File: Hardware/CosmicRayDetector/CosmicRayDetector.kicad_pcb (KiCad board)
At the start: 2 copper layers, 40 x 70 mm, 34 parts, among them J1 Conn_01x01_Female, J10 Conn_01x01_Female, J11 Conn_01x01_Female, J2 Conn_01x02, J6 Conn_01x04, J8 Conn_01x01_Female, J9 Conn_01x01_Female, U1 HEF4093B

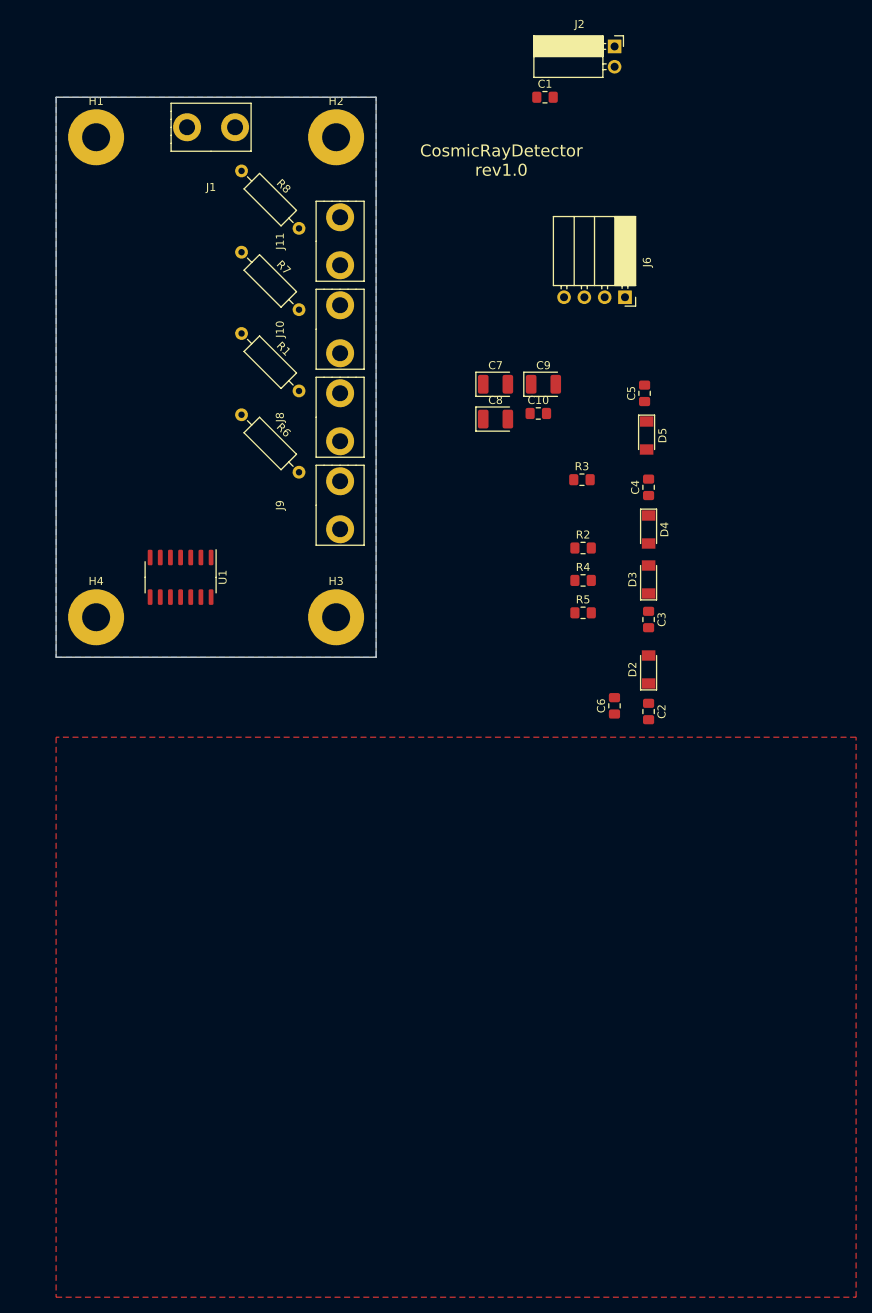
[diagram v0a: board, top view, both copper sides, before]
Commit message: done component placement on pcb and a draft of routing
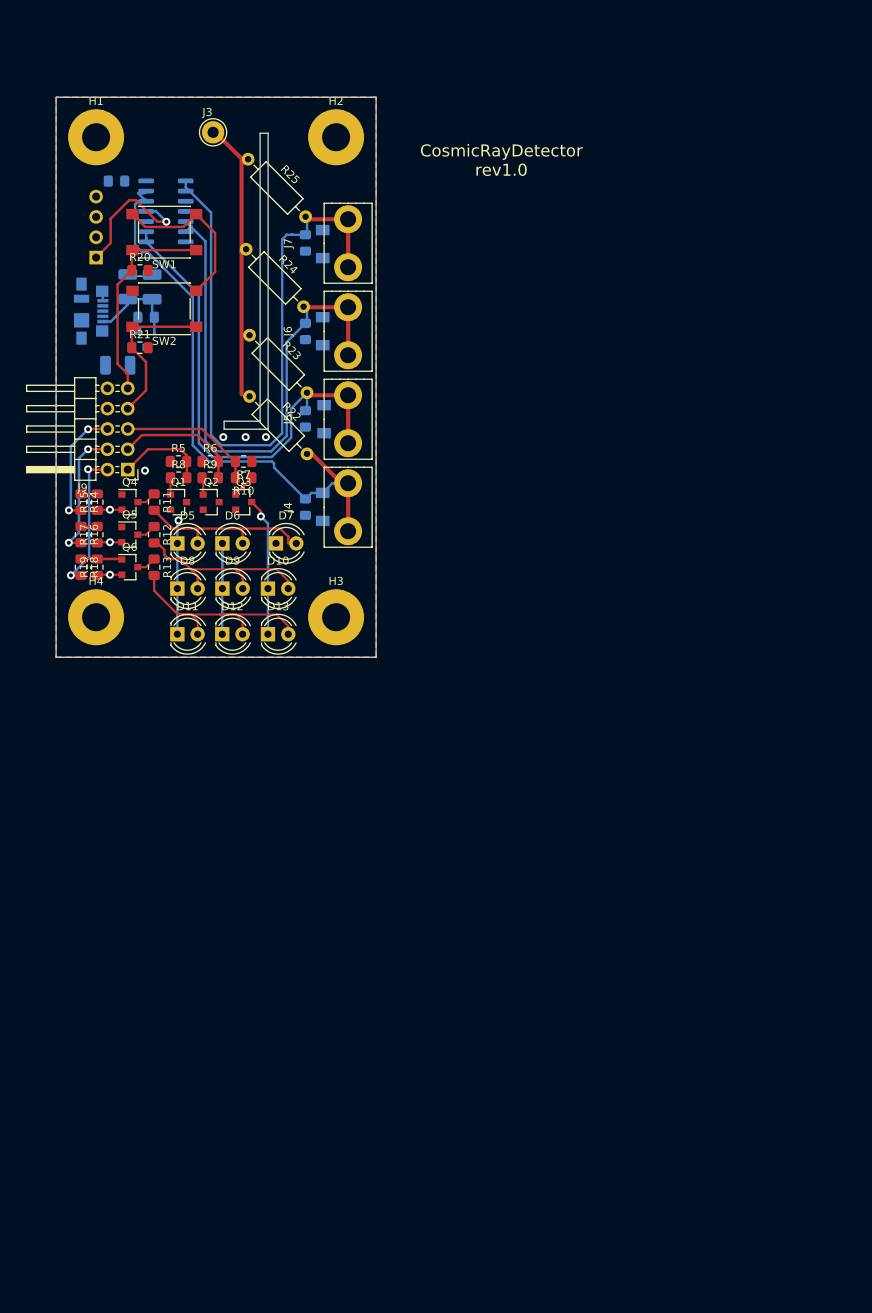
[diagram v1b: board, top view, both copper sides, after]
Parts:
- removed C10: 100n, Capacitor_SMD:C_0805_2012Metric_Pad1.15x1.40mm_HandSolder
- removed C2, C3, C4: 220p, Capacitor_SMD:C_0805_2012Metric_Pad1.15x1.40mm_HandSolder
- removed the C5 at (93.6, 57.0)
- removed J11: Conn_01x01_Female, CosmicRayDetector:GeigerTube
- removed J2: Conn_01x02, Connector_PinSocket_2.54mm:PinSocket_1x02_P2.54mm_Horizontal
- removed the J6 at (91.1, 45.0)
- added D1: 5V1, Diode_SMD:D_MiniMELF, B.Cu at (53.3, 71.2)
- added D10: LED, LED_THT:LED_D4.0mm, F.Cu at (46.5, 81.4)
- added D11: LED, LED_THT:LED_D4.0mm, F.Cu at (35.2, 87.1)
- added D12: LED, LED_THT:LED_D4.0mm, F.Cu at (40.8, 87.1)
- added D13: LED, LED_THT:LED_D4.0mm, F.Cu at (46.5, 87.1)
- added D6: LED, LED_THT:LED_D4.0mm, F.Cu at (40.8, 75.8)
- added D7: LED, LED_THT:LED_D4.0mm, F.Cu at (47.5, 75.8)
- added D8: LED, LED_THT:LED_D4.0mm, F.Cu at (35.2, 81.4)
- added D9: LED, LED_THT:LED_D4.0mm, F.Cu at (40.8, 81.4)
- added J1: Conn_01x04, Connector_PinSocket_2.54mm:PinSocket_1x04_P2.54mm_Horizontal, B.Cu at (25.0, 40.0)
- added J7: Conn_01x01_Female, CosmicRayDetector:GeigerTube, F.Cu at (48.5, 38.2)
- added J8: USB_B_Micro, Connector_USB:USB_Micro-B_Molex_47346-0001, B.Cu at (24.4, 46.7)
- added J9: Conn_02x05_Odd_Even, Connector_PinHeader_2.54mm:PinHeader_2x05_P2.54mm_Horizontal, F.Cu at (29.0, 66.5)
- added Q1: BC848, Package_TO_SOT_SMD:SOT-23, F.Cu at (35.3, 70.6)
- added Q2: BC848, Package_TO_SOT_SMD:SOT-23, F.Cu at (39.4, 70.6)
- added Q3: BC848, Package_TO_SOT_SMD:SOT-23, F.Cu at (43.5, 70.6)
- added Q4: BC859, Package_TO_SOT_SMD:SOT-23, F.Cu at (29.2, 70.6)
- added Q5: BC859, Package_TO_SOT_SMD:SOT-23, F.Cu at (29.2, 74.7)
- added Q6: BC859, Package_TO_SOT_SMD:SOT-23, F.Cu at (29.2, 78.7)
- added R10: 10k, Resistor_SMD:R_0805_2012Metric_Pad1.15x1.40mm_HandSolder, F.Cu at (43.4, 67.6)
- added R11: 10k, Resistor_SMD:R_0805_2012Metric_Pad1.15x1.40mm_HandSolder, F.Cu at (32.3, 70.6)
- added R12: 10k, Resistor_SMD:R_0805_2012Metric_Pad1.15x1.40mm_HandSolder, F.Cu at (32.3, 74.7)
- added R13: 10k, Resistor_SMD:R_0805_2012Metric_Pad1.15x1.40mm_HandSolder, F.Cu at (32.3, 78.7)
- added R14: 10k, Resistor_SMD:R_0805_2012Metric_Pad1.15x1.40mm_HandSolder, F.Cu at (23.1, 70.6)
- added R15: 10k, Resistor_SMD:R_0805_2012Metric_Pad1.15x1.40mm_HandSolder, F.Cu at (25.1, 70.6)
- added R16: 10k, Resistor_SMD:R_0805_2012Metric_Pad1.15x1.40mm_HandSolder, F.Cu at (23.1, 74.7)
- added R17: 10k, Resistor_SMD:R_0805_2012Metric_Pad1.15x1.40mm_HandSolder, F.Cu at (25.1, 74.7)
- added R18: 10k, Resistor_SMD:R_0805_2012Metric_Pad1.15x1.40mm_HandSolder, F.Cu at (23.1, 78.7)
- added R19: 10k, Resistor_SMD:R_0805_2012Metric_Pad1.15x1.40mm_HandSolder, F.Cu at (25.1, 78.7)
- added R2: 10k, Resistor_SMD:R_0805_2012Metric_Pad1.15x1.40mm_HandSolder, B.Cu at (51.2, 60.2)
- added R20: 10k, Resistor_SMD:R_0805_2012Metric_Pad1.15x1.40mm_HandSolder, F.Cu at (30.5, 41.7)
- added R21: 10k, Resistor_SMD:R_0805_2012Metric_Pad1.15x1.40mm_HandSolder, F.Cu at (30.5, 51.3)
- added R6: 10k, Resistor_SMD:R_0805_2012Metric_Pad1.15x1.40mm_HandSolder, F.Cu at (39.3, 65.5)
- added R7: 10k, Resistor_SMD:R_0805_2012Metric_Pad1.15x1.40mm_HandSolder, F.Cu at (43.4, 65.5)
- added R8: 10k, Resistor_SMD:R_0805_2012Metric_Pad1.15x1.40mm_HandSolder, F.Cu at (35.3, 67.6)
- added R9: 10k, Resistor_SMD:R_0805_2012Metric_Pad1.15x1.40mm_HandSolder, F.Cu at (39.3, 67.6)
- added SW1: SW_Push, Button_Switch_SMD:SW_SPST_PTS645, F.Cu at (33.5, 36.9)
- added SW2: SW_Push, Button_Switch_SMD:SW_SPST_PTS645, F.Cu at (33.5, 46.4)
- added U2: AZ1117-3.3, Package_TO_SOT_SMD:SOT-23, B.Cu at (30.2, 50.2)
- C5: renamed from C6; moved to B.Cu
- C6: renamed from C1; moved to B.Cu
- C7, C8, C9, D2, D3, D4, R3, R4, U1: moved to B.Cu
- D5: value 5V1 -> LED; footprint Diode_SMD:D_MiniMELF -> LED_THT:LED_D4.0mm
- J3: renamed from J1; footprint CosmicRayDetector:GeigerTube -> TestPoint:TestPoint_Loop_D2.60mm_Drill1.4mm_Beaded
- R1: renamed from R2; moved to B.Cu
- moved C5 90.4 mm to (27.6, 30.5), turned to 180 degrees
- moved D5 60.2 mm to (35.2, 75.8), turned to 0 degrees
- moved C6 56.9 mm to (31.2, 47.5), turned to 180 degrees
- moved R4 54.6 mm to (51.2, 38.2), turned to 270 degrees
- moved D4 54.2 mm to (53.3, 38.4)
- moved R5 54.0 mm to (35.3, 65.5)
- moved C9 53.3 mm to (27.7, 53.5), turned to 180 degrees
- moved D2 51.2 mm to (53.5, 60.2), turned to 270 degrees
- moved D3 51.2 mm to (53.3, 49.2), turned to 270 degrees
- moved C8 48.9 mm to (29.0, 43.7), turned to 90 degrees
- moved U1 45.8 mm to (33.7, 34.3), turned to 180 degrees
- moved C7 44.6 mm to (32.0, 43.7), turned to 90 degrees
- moved R3 39.2 mm to (51.2, 49.3), turned to 270 degrees
- moved R1 35.1 mm to (51.2, 71.2), turned to 270 degrees
- moved J4 11.3 mm to (48.5, 71.2)
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- renumbered J8 to J4, J9 to J5, J10 to J6, R1 to R22, R6 to R23, R7 to R24, R8 to R25
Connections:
- C5 pad 1: VCC -> +3V3
- D2 pad 1: GM_CONNECTOR_1 -> GM_CONNECTOR_2
- D3 pad 1: GM_CONNECTOR_2 -> GM_CONNECTOR_3
- D4 pad 1: GM_CONNECTOR_3 -> GM_CONNECTOR_4
- D5 pad 1: GM_CONNECTOR_4 -> Net-(D11-Pad1)
- D5 pad 2: GND -> Net-(D5-Pad2)
- R3 pad 1: GM_CONNECTOR_2 -> GM_CONNECTOR_3
- R4 pad 1: GM_CONNECTOR_3 -> GM_CONNECTOR_4
- R5 pad 1: GM_CONNECTOR_4 -> GND
- R5 pad 2: GND -> /UserInterface/LED_X_3
- U1 pad 1: GM_CONNECTOR_3 -> GM_CONNECTOR_4
- U1 pad 10: GM1 -> Net-(J1-Pad2)
- U1 pad 11: GM2 -> Net-(J1-Pad1)
- U1 pad 12: GM_CONNECTOR_2 -> GM_CONNECTOR_1
- U1 pad 13: GM_CONNECTOR_2 -> GM_CONNECTOR_1
- U1 pad 14: VCC -> +3V3
- U1 pad 2: GM_CONNECTOR_3 -> GM_CONNECTOR_4
- U1 pad 3: GM3 -> Net-(J1-Pad4)
- U1 pad 4: GM4 -> Net-(J1-Pad3)
- U1 pad 5: GM_CONNECTOR_4 -> GM_CONNECTOR_3
- U1 pad 6: GM_CONNECTOR_4 -> GM_CONNECTOR_3
- U1 pad 8: GM_CONNECTOR_1 -> GM_CONNECTOR_2
- U1 pad 9: GM_CONNECTOR_1 -> GM_CONNECTOR_2
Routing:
- net GM_CONNECTOR_4: track 0.00 -> 85.1 mm
- net GM_CONNECTOR_1: track 0.00 -> 73.9 mm
- net GM_CONNECTOR_3: track 0.00 -> 70.3 mm
- net GM_CONNECTOR_2: track 0.00 -> 63.6 mm
- net Net-(J3-Pad1): track 0.00 -> 33.9 mm
- net Net-(D11-Pad2): track 0.00 -> 30.8 mm
- net /UserInterface/BUTTON_1: track 0.00 -> 26.5 mm
- net Net-(D10-Pad2): track 0.00 -> 25.6 mm
- net Net-(D5-Pad2): track 0.00 -> 23.9 mm
- net +5V: track 0.00 -> 23.8 mm, vias 0 -> 3
- net +3V3: track 0.00 -> 20.8 mm
- net /UserInterface/BUTTON_2: track 0.00 -> 19.9 mm
- net /UserInterface/LED_Y_3: track 0.00 -> 18.3 mm, vias 0 -> 2
- net Net-(J1-Pad1): track 0.00 -> 17.7 mm, vias 0 -> 1
- net Net-(D10-Pad1): track 0.00 -> 17.4 mm, vias 0 -> 1
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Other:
- outline, holes or cut-outs redrawn
- net class Default: clearance 0.254 -> 0.1778
- net class high voltage: clearance 2 -> 0.254; trace_width 0.3048 -> 2
- rule trace_clearance: 0.254 -> 0.1778

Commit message: finished pcb design
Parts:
- removed J9: Conn_02x05_Odd_Even, Connector_PinHeader_2.54mm:PinHeader_2x05_P2.54mm_Horizontal
- added C2: 100n, Capacitor_SMD:C_0805_2012Metric_Pad1.15x1.40mm_HandSolder, F.Cu at (30.0, 65.5)
- added D14: LED, LED_THT:LED_D4.0mm, F.Cu at (34.5, 72.1)
- added D15: LED, LED_THT:LED_D4.0mm, F.Cu at (39.4, 72.1)
- added D16: LED, LED_THT:LED_D4.0mm, F.Cu at (44.2, 72.1)
- added D17: LED, LED_THT:LED_D4.0mm, F.Cu at (49.0, 87.2)
- added D18: LED, LED_THT:LED_D4.0mm, F.Cu at (49.0, 82.2)
- added D19: LED, LED_THT:LED_D4.0mm, F.Cu at (49.0, 77.1)
- added D20: LED, LED_THT:LED_D4.0mm, F.Cu at (49.0, 72.1)
- added J2: Conn_02x06_Odd_Even, Connector_PinHeader_2.54mm:PinHeader_2x06_P2.54mm_Horizontal, F.Cu at (27.7, 63.0)
- added Q7: BC848, Package_TO_SOT_SMD:SOT-23, F.Cu at (28.0, 68.1)
- added Q8: BC859, Package_TO_SOT_SMD:SOT-23, F.Cu at (45.2, 66.8)
- added R26: 10k, Resistor_SMD:R_0402_1005Metric, F.Cu at (24.9, 68.6)
- added R27: 10k, Resistor_SMD:R_0402_1005Metric, F.Cu at (24.9, 67.1)
- added R28: 10k, Resistor_SMD:R_0402_1005Metric, F.Cu at (46.2, 64.3)
- added R29: 10k, Resistor_SMD:R_0402_1005Metric, F.Cu at (44.2, 64.3)
- added R30: 10k, Resistor_SMD:R_0805_2012Metric_Pad1.15x1.40mm_HandSolder, F.Cu at (45.2, 69.6)
- J1: footprint Connector_PinSocket_2.54mm:PinSocket_1x04_P2.54mm_Horizontal -> Connector_PinHeader_2.54mm:PinHeader_1x04_P2.54mm_Horizontal
- R10, R14, R15, R16, R17, R18, R19, R5, R6, R7, R8, R9: footprint Resistor_SMD:R_0805_2012Metric_Pad1.15x1.40mm_HandSolder -> Resistor_SMD:R_0402_1005Metric
- moved C5 39.4 mm to (35.9, 69.0)
- moved U1 33.3 mm to (42.5, 66.4), turned to 270 degrees
- moved R18 23.9 mm to (42.2, 64.3), turned to 0 degrees
- moved R19 20.8 mm to (40.1, 64.3), turned to 0 degrees
- moved R7 19.7 mm to (24.9, 72.1)
- moved R10 18.8 mm to (24.9, 70.6)
- moved R16 18.2 mm to (38.1, 64.3), turned to 0 degrees
- moved R6 17.6 mm to (24.9, 75.7), turned to 180 degrees
- moved R5 17.2 mm to (24.9, 79.2), turned to 180 degrees
- moved Q6 16.9 mm to (41.1, 66.8), turned to 270 degrees
- moved C9 16.2 mm to (36.1, 39.6), turned to 0 degrees
- moved R9 15.8 mm to (24.9, 74.2), turned to 180 degrees
- moved Q3 15.5 mm to (27.9, 71.6)
- moved R17 15.1 mm to (36.1, 64.3), turned to 0 degrees
- moved U2 15.1 mm to (36.1, 36.3)
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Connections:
- R10 pad 2: /UserInterface/LED_X_1 -> /UserInterface/LED_X_3
- R5 pad 2: /UserInterface/LED_X_3 -> /UserInterface/LED_X_1
- R7 pad 2: /UserInterface/LED_X_1 -> /UserInterface/LED_X_3
- R8 pad 2: /UserInterface/LED_X_3 -> /UserInterface/LED_X_1
- U1 pad 10: Net-(J1-Pad2) -> Net-(J1-Pad3)
- U1 pad 11: Net-(J1-Pad1) -> Net-(J1-Pad4)
- U1 pad 3: Net-(J1-Pad4) -> Net-(J1-Pad1)
- U1 pad 4: Net-(J1-Pad3) -> Net-(J1-Pad2)
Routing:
- net +5V: track 23.8 -> 80.0 mm, vias 3 -> 1
- net GM_CONNECTOR_1: track 73.9 -> 34.3 mm
- net Net-(J1-Pad3): track 0.02 -> 35.1 mm
- net Net-(J1-Pad2): track 0.22 -> 34.5 mm
- net Net-(D14-Pad1): track 0.00 -> 33.3 mm
- net Net-(J1-Pad4): track 0.00 -> 32.8 mm
- net GM_CONNECTOR_2: track 63.6 -> 32.9 mm
- net GM_CONNECTOR_4: track 85.1 -> 56.4 mm
- net GM_CONNECTOR_3: track 70.3 -> 44.9 mm
- net /UserInterface/LED_Y_4: track 0.00 -> 25.0 mm
- net +3V3: track 20.8 -> 44.5 mm, vias 0 -> 2
- net Net-(D12-Pad1): track 11.4 -> 32.4 mm
- net Net-(D11-Pad1): track 14.0 -> 33.9 mm, vias 1 -> 0
- net Net-(D17-Pad2): track 0.00 -> 18.7 mm
- net Net-(J1-Pad1): track 17.7 -> 33.9 mm, vias 1 -> 0
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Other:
- net class high voltage: clearance 0.254 -> 0.75

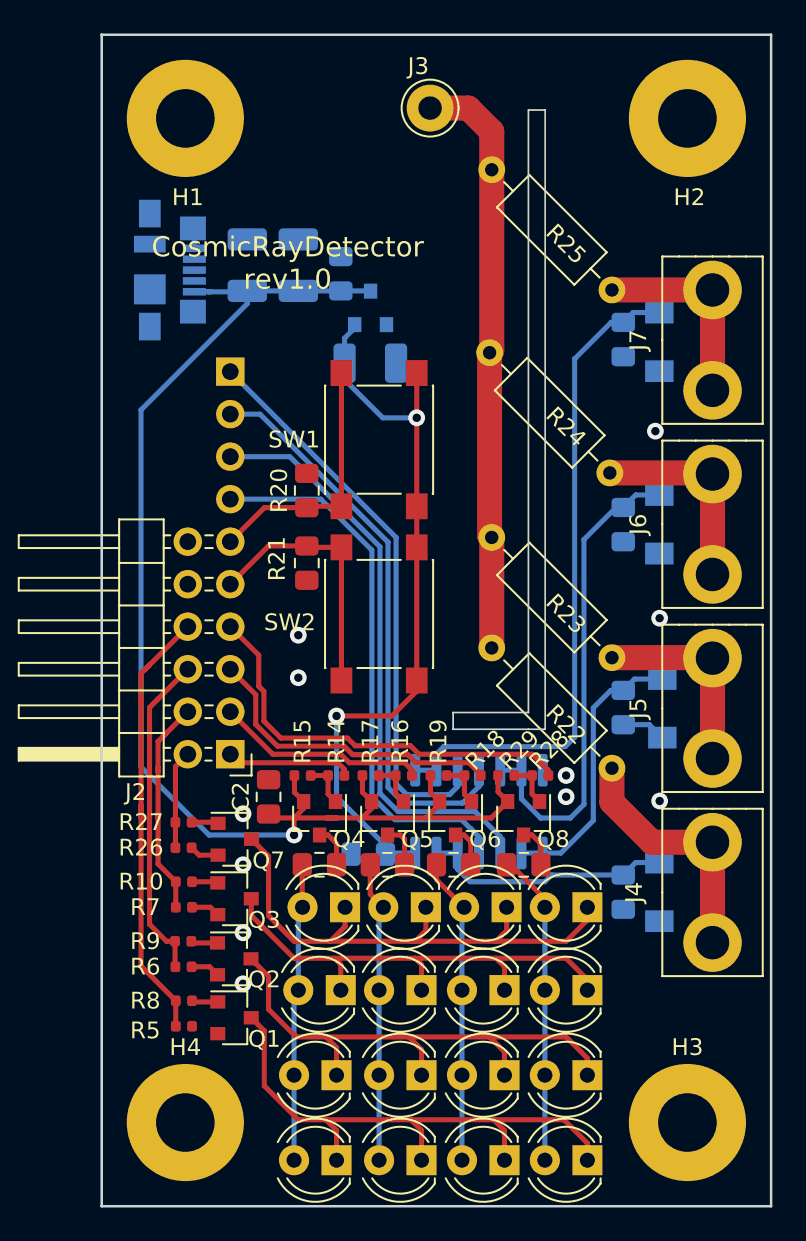
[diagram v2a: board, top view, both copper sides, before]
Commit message: Improve PCB design (fix: #97)
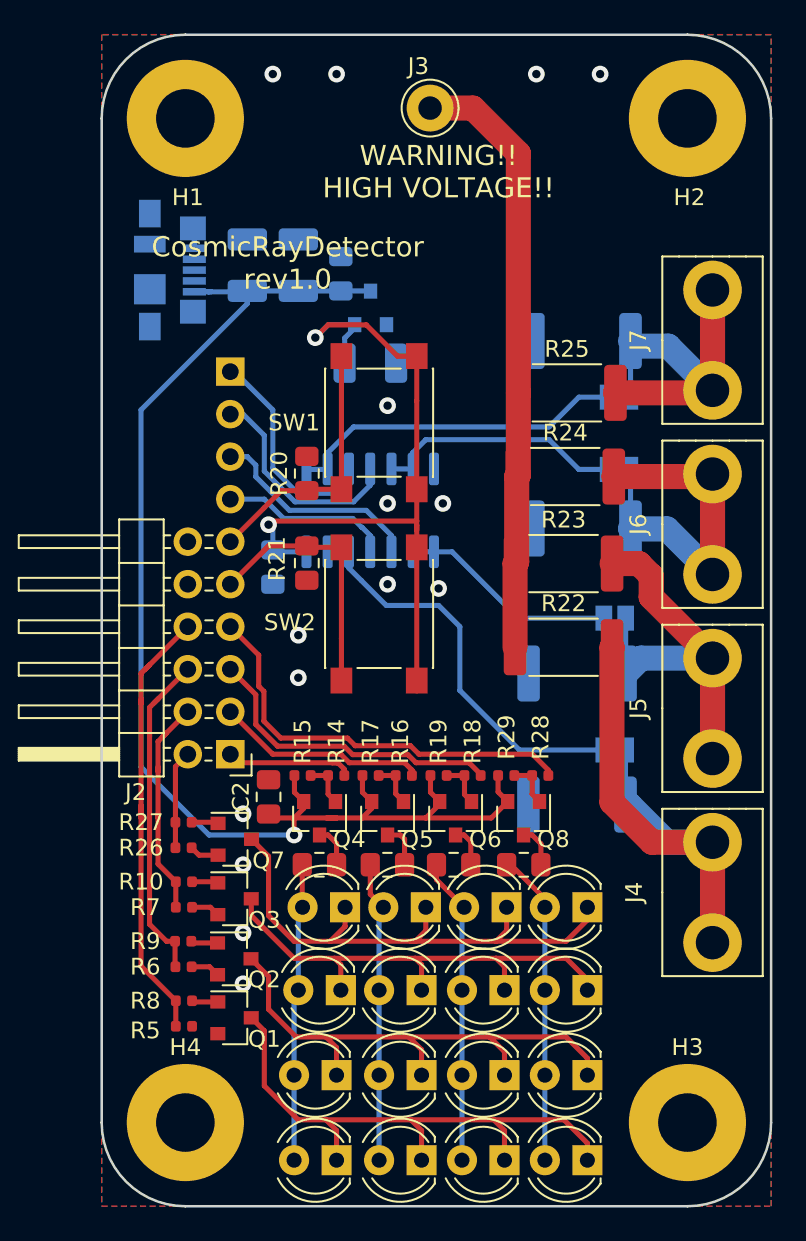
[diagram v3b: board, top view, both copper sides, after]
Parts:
- removed D1, D2, D3, D4: 5V1, Diode_SMD:D_MiniMELF
- added JP1: Jumper_NO_Small, Jumper:SolderJumper-2_P1.3mm_Open_Pad1.0x1.5mm, B.Cu at (50.9, 41.7)
- added JP2: Jumper_NO_Small, Jumper:SolderJumper-2_P1.3mm_Open_Pad1.0x1.5mm, B.Cu at (50.7, 62.7)
- added JP3: Jumper_NO_Small, Jumper:SolderJumper-2_P1.3mm_Open_Pad1.0x1.5mm, B.Cu at (50.7, 54.9)
- added JP4: Jumper_NO_Small, Jumper:SolderJumper-2_P1.3mm_Open_Pad1.0x1.5mm, B.Cu at (50.9, 46.0)
- R1, R2, R3, R4: footprint Resistor_SMD:R_0805_2012Metric_Pad1.15x1.40mm_HandSolder -> Resistor_SMD:R_2512_6332Metric
- R22, R23, R24, R25: footprint Resistor_THT:R_Axial_DIN0207_L6.3mm_D2.5mm_P10.16mm_Horizontal -> Resistor_SMD:R_2512_6332Metric
- moved U1 19.1 mm to (36.0, 48.4)
- moved C5 18.1 mm to (30.2, 51.8), turned to 270 degrees
- moved R25 14.1 mm to (47.8, 41.4), turned to 0 degrees
- moved R24 8.67 mm to (47.7, 46.4), turned to 0 degrees
- moved R1 5.92 mm to (48.4, 66.0), turned to 180 degrees
- moved R23 4.57 mm to (47.6, 51.6), turned to 0 degrees
- moved R22 4.29 mm to (47.6, 56.6), turned to 0 degrees
- moved R2 3.43 mm to (48.4, 58.2), turned to 180 degrees
- moved R3 2.48 mm to (48.7, 49.5), turned to 180 degrees
- moved R4 2.47 mm to (48.7, 38.3), turned to 180 degrees
- moved R20 1.02 mm to (32.3, 46.2)
- moved SW1 1.02 mm to (36.6, 43.2)
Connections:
- net Net-(J3-Pad1) renamed /HVConnector/HIGH_VOLTAGE
- U1 pad 1: GM_CONNECTOR_4 -> Net-(JP1-Pad2)
- U1 pad 12: GM_CONNECTOR_1 -> Net-(JP2-Pad2)
- U1 pad 13: GM_CONNECTOR_1 -> Net-(JP2-Pad2)
- U1 pad 2: GM_CONNECTOR_4 -> Net-(JP1-Pad2)
- U1 pad 5: GM_CONNECTOR_3 -> Net-(JP4-Pad2)
- U1 pad 6: GM_CONNECTOR_3 -> Net-(JP4-Pad2)
- U1 pad 8: GM_CONNECTOR_2 -> Net-(JP3-Pad2)
- U1 pad 9: GM_CONNECTOR_2 -> Net-(JP3-Pad2)
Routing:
- net GM_CONNECTOR_4: track 56.4 -> 21.4 mm
- net Net-(JP2-Pad2): track 0.00 -> 24.2 mm
- net GM_CONNECTOR_3: track 44.9 -> 21.6 mm
- net Net-(J1-Pad4): track 32.8 -> 10.2 mm
- net Net-(J1-Pad3): track 35.1 -> 13.0 mm
- net Net-(J1-Pad2): track 34.5 -> 13.2 mm, vias 0 -> 1
- net Net-(J1-Pad1): track 33.9 -> 13.3 mm
- net Net-(JP1-Pad2): track 0.00 -> 20.4 mm
- net Net-(JP4-Pad2): track 0.00 -> 15.0 mm
- net Net-(JP3-Pad2): track 0.00 -> 13.1 mm
- net GM_CONNECTOR_2: track 32.9 -> 24.3 mm
- net GND: track 9.11 -> 6.45 mm, vias 11 -> 15
- net GM_CONNECTOR_1: track 34.3 -> 31.7 mm
- net +3V3: track 44.5 -> 46.3 mm
- net /HVConnector/HIGH_VOLTAGE: track 35.5 -> 36.2 mm
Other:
- outline, holes or cut-outs redrawn
- net class high voltage: clearance 0.75 -> 2.75
- board text added: "WARNING!! HIGH VOLTAGE!!"
